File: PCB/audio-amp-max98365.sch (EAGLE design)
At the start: 20 parts, among them U1 MAX98365

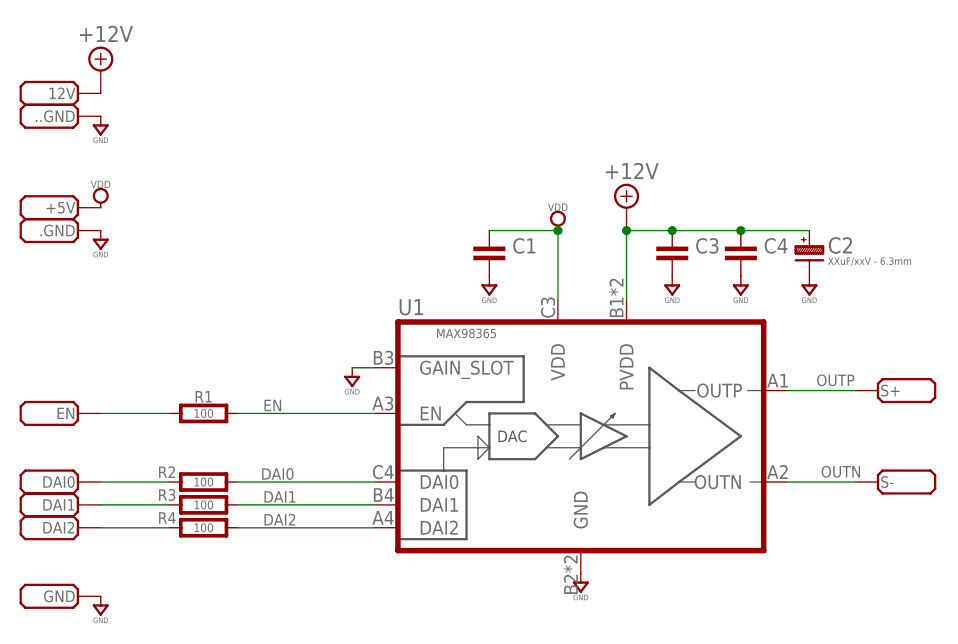
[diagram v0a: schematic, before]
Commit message: Added BOM. Updated missing component values.
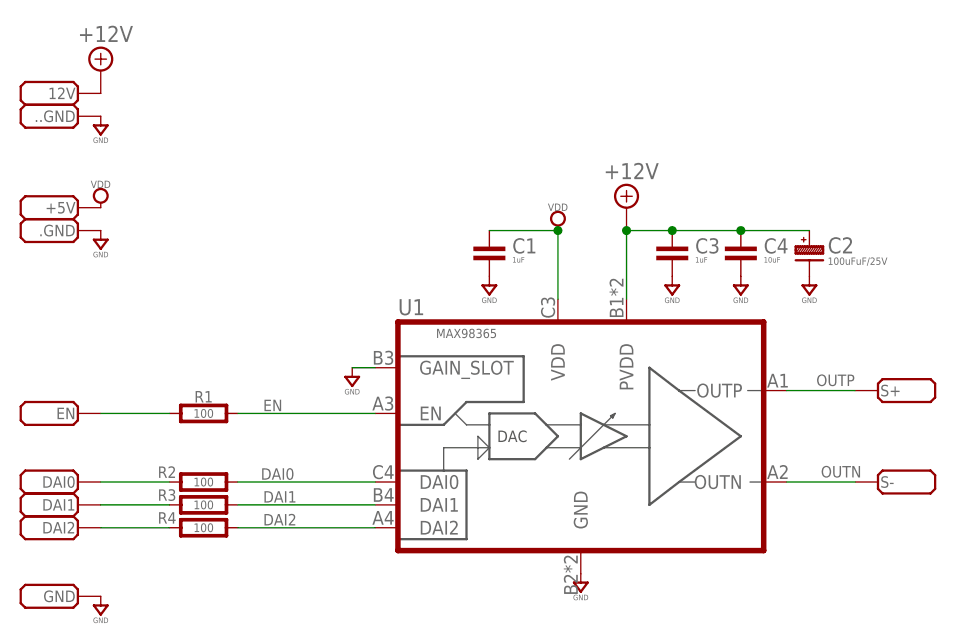
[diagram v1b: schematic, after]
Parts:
- C1, C3: value (none) -> 1uF
- C2: value XXuF/xxV - 6.3mm -> 100uFuF/25V
- C4: value (none) -> 10uF
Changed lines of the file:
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@@
 <part name="S+" library="con-testpoints" library_urn="urn:adsk.eagle:library:7289188" deviceset="PAD" device="SMD-100X100" package3d_urn="urn:adsk.eagle:package:12570102/4" value="PADSMD-100X100"/>
 <part name="S-" library="con-testpoints" library_urn="urn:adsk.eagle:library:7289188" deviceset="PAD" device="SMD-100X100" package3d_urn="urn:adsk.eagle:package:12570102/4" value="PADSMD-100X100"/>
-<part name="C1" library="rlc" library_urn="urn:adsk.eagle:library:4192893" deviceset="CAPACITOR" device="0603" package3d_urn="urn:adsk.eagle:package:4193021/2"/>
-<part name="C2" library="rlc" library_urn="urn:adsk.eagle:library:4192893" deviceset="CAPACITOR_POL" device="-ALUM-SMT-6.3" package3d_urn="urn:adsk.eagle:package:4192955/2" value="XXuF/xxV - 6.3mm"/>
+<part name="C1" library="rlc" library_urn="urn:adsk.eagle:library:4192893" deviceset="CAPACITOR" device="0603" package3d_urn="urn:adsk.eagle:package:4193021/2" value="1uF"/>
+<part name="C2" library="rlc" library_urn="urn:adsk.eagle:library:4192893" deviceset="CAPACITOR_POL" device="-ALUM-SMT-6.3" package3d_urn="urn:adsk.eagle:package:4192955/2" value="100uFuF/25V"/>
 <part name="R1" library="rlc" library_urn="urn:adsk.eagle:library:4192893" deviceset="RESISTOR" device="0603" package3d_urn="urn:adsk.eagle:package:4193040/2" value="100"/>
 <part name="SUPPLY1" library="supply" library_urn="urn:adsk.eagle:library:10485988" deviceset="VDD" device=""/>
@@
 <part name="R4" library="rlc" library_urn="urn:adsk.eagle:library:4192893" deviceset="RESISTOR" device="0603" package3d_urn="urn:adsk.eagle:package:4193040/2" value="100"/>
 <part name="DAI2" library="con-testpoints" library_urn="urn:adsk.eagle:library:7289188" deviceset="PAD" device="SMD-070X070" package3d_urn="urn:adsk.eagle:package:16261575/3"/>
-<part name="C3" library="rlc" library_urn="urn:adsk.eagle:library:4192893" deviceset="CAPACITOR" device="0603" package3d_urn="urn:adsk.eagle:package:4193021/2"/>
-<part name="C4" library="rlc" library_urn="urn:adsk.eagle:library:4192893" deviceset="CAPACITOR" device="0603" package3d_urn="urn:adsk.eagle:package:4193021/2"/>
+<part name="C3" library="rlc" library_urn="urn:adsk.eagle:library:4192893" deviceset="CAPACITOR" device="0603" package3d_urn="urn:adsk.eagle:package:4193021/2" value="1uF"/>
+<part name="C4" library="rlc" library_urn="urn:adsk.eagle:library:4192893" deviceset="CAPACITOR" device="0603" package3d_urn="urn:adsk.eagle:package:4193021/2" value="10uF"/>
 <part name="SUPPLY5" library="supply" library_urn="urn:adsk.eagle:library:10485988" deviceset="GND" device=""/>
 <part name="SUPPLY6" library="supply" library_urn="urn:adsk.eagle:library:10485988" deviceset="GND" device=""/>
